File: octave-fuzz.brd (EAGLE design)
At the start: 100 x 81.3 mm, 56 parts, among them T1 2N5089, T2 2N5089, T3 2N5089, T4 2N5089, T5 2N5089

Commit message: optimized layout
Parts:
- moved R5 37.2 mm to (55.9, 47.0), turned to 180 degrees
- moved POT_VOL1 29.0 mm to (72.4, 48.3)
- moved D6 26.8 mm to (72.4, 33.0)
- moved D7 26.8 mm to (67.3, 33.0)
- moved POT_VOL2 26.8 mm to (67.3, 44.5)
- moved R14 25.4 mm to (74.9, 20.3), turned to 90 degrees
- moved POT_GAIN1_2 25.2 mm to (72.4, 55.9), turned to 0 degrees
- moved T2 24.2 mm to (64.8, 58.4)
- moved C3 24.2 mm to (63.5, 64.8)
- moved POT_GAIN1 24.2 mm to (68.6, 62.2)
- moved R21 24.2 mm to (72.4, 69.8)
- moved C7 22.9 mm to (62.2, 72.4)
- moved C9 22.9 mm to (29.2, 29.2), turned to 90 degrees
- moved D5 22.2 mm to (63.5, 38.1)
- moved T3 22.2 mm to (33.0, 63.5)
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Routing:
- net GND: track 265.5 -> 208.3 mm
- net N$5: track 67.4 -> 27.7 mm
- net N$3: track 65.0 -> 36.0 mm
- net +9V: track 257.9 -> 276.9 mm
- net N$26: track 24.8 -> 36.8 mm
- net N$4: track 0.00 -> 11.1 mm
- net N$30: track 10.7 -> 20.9 mm
- net N$23: track 28.8 -> 20.5 mm
- net N$22: track 11.0 -> 17.0 mm
- net N$28: track 23.9 -> 29.8 mm
- net N$2: track 38.4 -> 44.0 mm
- net N$6: track 0.00 -> 4.86 mm
- net N$10: track 17.1 -> 13.3 mm
- net 4.5V: track 22.2 -> 18.6 mm
- net N$14: track 38.4 -> 35.0 mm
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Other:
- board size 100 x 81.3 mm -> 77.1 x 81.3 mm

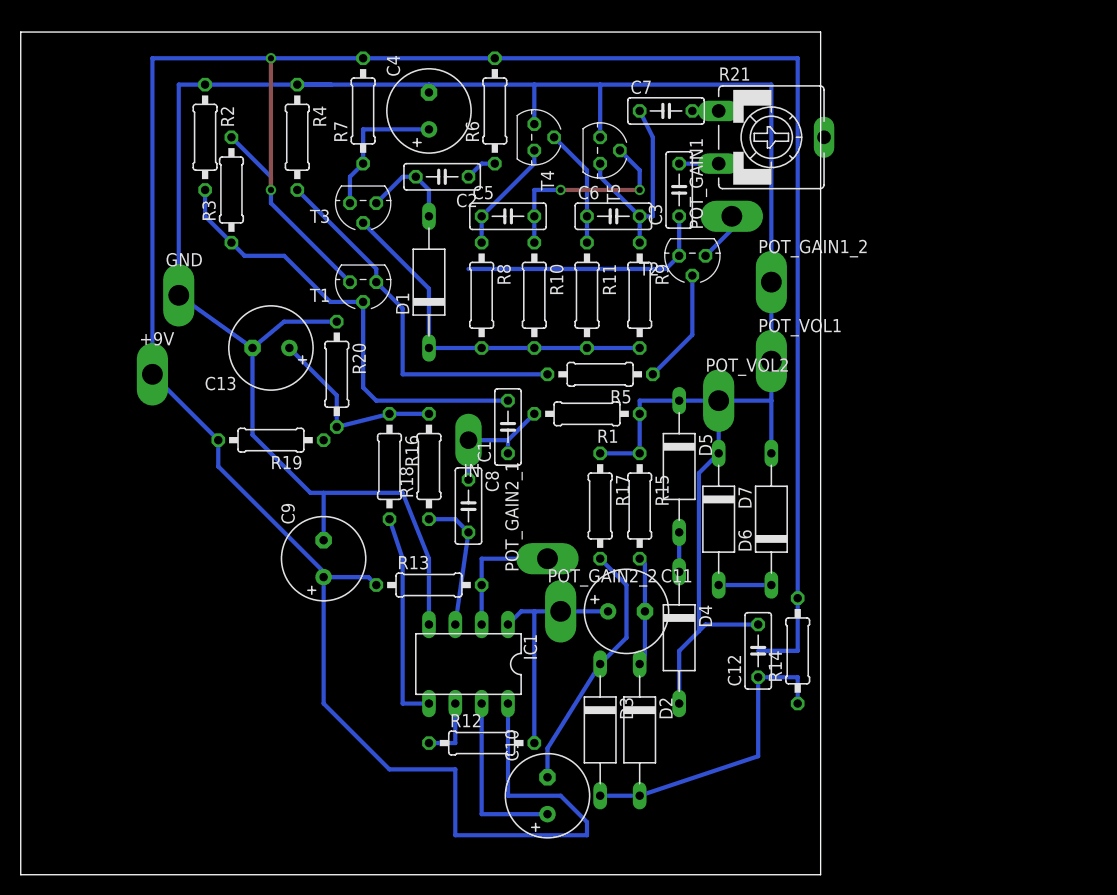
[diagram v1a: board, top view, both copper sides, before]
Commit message: improved pcb layout
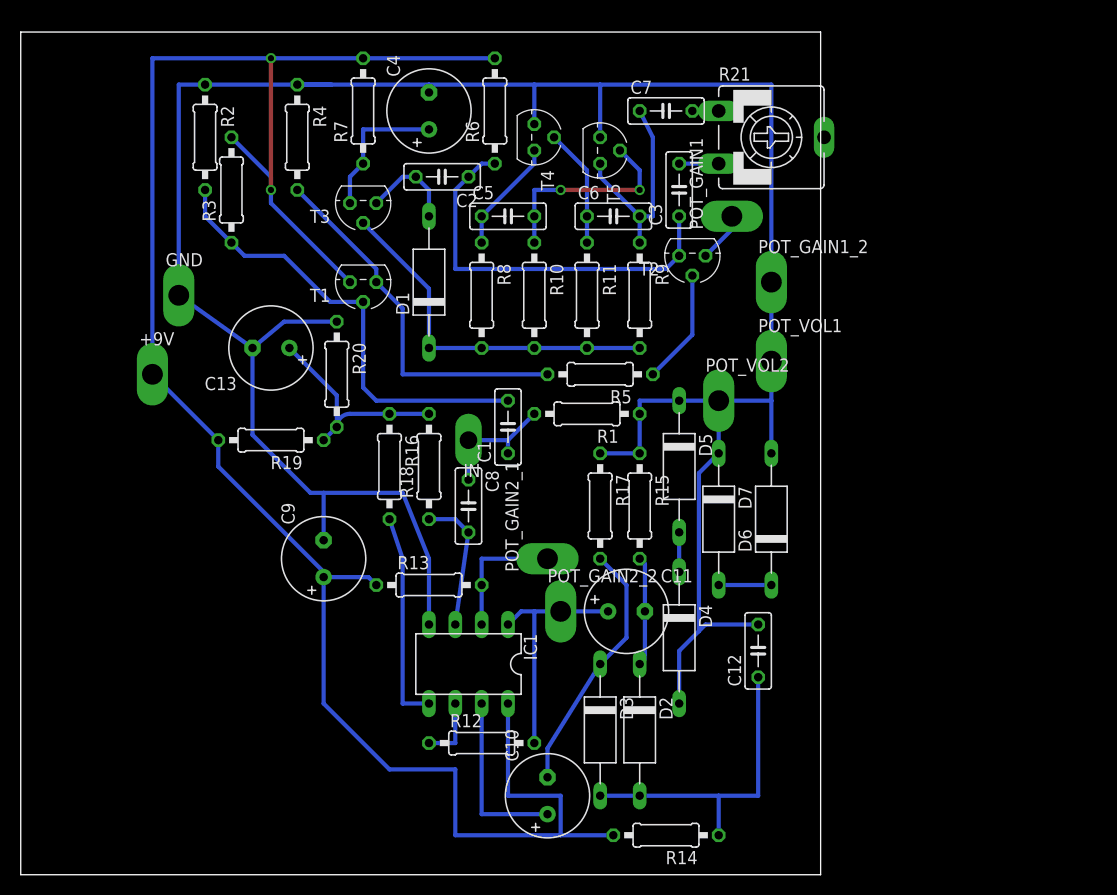
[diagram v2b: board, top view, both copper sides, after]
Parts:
- moved R14 21.8 mm to (62.2, 2.54), turned to 180 degrees
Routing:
- net +9V: track 276.9 -> 188.2 mm
- net N$5: track 27.7 -> 38.4 mm
- net 4.5V: track 18.6 -> 20.7 mm
- net N$28: track 29.8 -> 30.5 mm
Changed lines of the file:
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@@
 <layer number="23" name="tOrigins" color="15" fill="1" visible="yes" active="yes"/>
 <layer number="24" name="bOrigins" color="15" fill="1" visible="yes" active="yes"/>
-<layer number="25" name="tNames" color="7" fill="1" visible="no" active="yes"/>
-<layer number="26" name="bNames" color="7" fill="1" visible="no" active="yes"/>
+<layer number="25" name="tNames" color="7" fill="1" visible="yes" active="yes"/>
+<layer number="26" name="bNames" color="7" fill="1" visible="yes" active="yes"/>
 <layer number="27" name="tValues" color="7" fill="1" visible="no" active="yes"/>
 <layer number="28" name="bValues" color="7" fill="1" visible="no" active="yes"/>
@@
 <element name="R12" library="resistor" package="0207/10" value="" x="44.45" y="11.43"/>
 <element name="R13" library="resistor" package="0207/10" value="" x="39.37" y="26.67"/>
-<element name="R14" library="resistor" package="0207/10" value="" x="74.93" y="20.32" rot="R90"/>
+<element name="R14" library="resistor" package="0207/10" value="" x="62.23" y="2.54" rot="R180"/>
 <element name="R15" library="resistor" package="0207/10" value="" x="59.69" y="34.29" rot="R270"/>
 <element name="R16" library="resistor" package="0207/10" value="" x="35.56" y="38.1" rot="R270"/>
@@
 <wire x1="12.7" y1="46.99" x2="12.7" y2="77.47" width="0.4064" layer="16"/>
 <wire x1="12.7" y1="77.47" x2="24.13" y2="77.47" width="0.4064" layer="16"/>
-<wire x1="24.13" y1="77.47" x2="74.93" y2="77.47" width="0.4064" layer="16"/>
 <via x="24.13" y="64.77" extent="1-16" drill="0.6" shape="square"/>
 <via x="24.13" y="77.47" extent="1-16" drill="0.6" shape="square"/>
 <wire x1="24.13" y1="64.77" x2="24.13" y2="77.47" width="0.4064" layer="1"/>
-<wire x1="74.93" y1="25.4" x2="74.93" y2="77.47" width="0.4064" layer="16"/>
-<wire x1="74.93" y1="25.4" x2="74.93" y2="20.32" width="0.4064" layer="16"/>
-<wire x1="74.93" y1="20.32" x2="71.12" y2="20.32" width="0.4064" layer="16"/>
 <wire x1="31.75" y1="55.88" x2="24.13" y2="63.5" width="0.4064" layer="16"/>
 <wire x1="24.13" y1="63.5" x2="24.13" y2="64.77" width="0.4064" layer="16"/>
@@
 <wire x1="35.56" y1="8.89" x2="41.91" y2="8.89" width="0.4064" layer="16"/>
 <wire x1="41.91" y1="8.89" x2="41.91" y2="2.54" width="0.4064" layer="16"/>
-<wire x1="41.91" y1="2.54" x2="54.61" y2="2.54" width="0.4064" layer="16"/>
-<wire x1="54.61" y1="2.54" x2="54.61" y2="3.81" width="0.4064" layer="16"/>
-<wire x1="54.61" y1="3.81" x2="52.07" y2="6.35" width="0.4064" layer="16"/>
+<wire x1="41.91" y1="2.54" x2="52.07" y2="2.54" width="0.4064" layer="16"/>
+<wire x1="52.07" y1="2.54" x2="52.07" y2="6.35" width="0.4064" layer="16"/>
 <wire x1="52.07" y1="6.35" x2="46.99" y2="6.35" width="0.4064" layer="16"/>
 <wire x1="46.99" y1="6.35" x2="46.99" y2="15.24" width="0.4064" layer="16"/>
@@
 <wire x1="19.05" y1="38.1" x2="29.21" y2="27.94" width="0.4064" layer="16"/>
 <wire x1="29.21" y1="27.94" x2="29.21" y2="15.24" width="0.4064" layer="16"/>
-<wire x1="33.02" y1="77.47" x2="45.72" y2="77.47" width="0" layer="19" extent="1-1"/>
-<wire x1="24.13" y1="77.47" x2="33.02" y2="77.47" width="0" layer="19" extent="16-16"/>
+<wire x1="52.07" y1="2.54" x2="57.15" y2="2.54" width="0.4064" layer="16"/>
+<wire x1="24.13" y1="77.47" x2="33.02" y2="77.47" width="0.4064" layer="16"/>
+<wire x1="33.02" y1="77.47" x2="45.72" y2="77.47" width="0.4064" layer="16"/>
 </signal>
 <signal name="N$2">
@@
 <wire x1="63.5" y1="62.23" x2="63.5" y2="58.42" width="0.4064" layer="16"/>
 <wire x1="63.5" y1="58.42" x2="62.23" y2="57.15" width="0.4064" layer="16"/>
-<wire x1="62.23" y1="57.15" x2="43.18" y2="57.15" width="0.4064" layer="16"/>
+<wire x1="62.23" y1="57.15" x2="41.91" y2="57.15" width="0.4064" layer="16"/>
 <wire x1="43.18" y1="66.04" x2="44.45" y2="67.31" width="0.4064" layer="16"/>
 <wire x1="44.45" y1="67.31" x2="45.72" y2="67.31" width="0.4064" layer="16"/>
-<wire x1="43.18" y1="57.15" x2="43.18" y2="66.04" width="0" layer="19" extent="16-16"/>
+<wire x1="41.91" y1="57.15" x2="41.91" y2="64.77" width="0.4064" layer="16"/>
+<wire x1="41.91" y1="64.77" x2="43.18" y2="66.04" width="0.4064" layer="16"/>
 </signal>
 <signal name="N$6">
@@
 <contactref element="C12" pad="1"/>
 <wire x1="55.88" y1="6.35" x2="59.69" y2="6.35" width="0.4064" layer="16"/>
-<wire x1="59.69" y1="6.35" x2="71.12" y2="10.16" width="0.4064" layer="16"/>
-<wire x1="71.12" y1="10.16" x2="71.12" y2="17.78" width="0.4064" layer="16"/>
-<wire x1="71.12" y1="17.78" x2="74.93" y2="17.78" width="0.4064" layer="16"/>
-<wire x1="74.93" y1="17.78" x2="74.93" y2="15.24" width="0.4064" layer="16"/>
+<wire x1="59.69" y1="6.35" x2="67.31" y2="6.35" width="0.4064" layer="16"/>
+<wire x1="67.31" y1="6.35" x2="71.12" y2="6.35" width="0.4064" layer="16"/>
+<wire x1="71.12" y1="6.35" x2="71.12" y2="17.78" width="0.4064" layer="16"/>
+<wire x1="67.31" y1="2.54" x2="67.31" y2="6.35" width="0.4064" layer="16"/>
 </signal>
 <signal name="N$27">
@@
 <contactref element="R20" pad="2"/>
 <contactref element="C13" pad="+"/>
-<wire x1="35.56" y1="43.18" x2="30.48" y2="41.91" width="0.4064" layer="16"/>
 <wire x1="25.908" y1="49.53" x2="30.48" y2="44.958" width="0.4064" layer="16"/>
 <wire x1="30.48" y1="44.958" x2="30.48" y2="41.91" width="0.4064" layer="16"/>
 <wire x1="35.56" y1="43.18" x2="39.37" y2="43.18" width="0.4064" layer="16"/>
-<wire x1="29.21" y1="40.64" x2="30.48" y2="41.91" width="0" layer="19" extent="1-1"/>
+<wire x1="35.56" y1="43.18" x2="31.75" y2="43.18" width="0.4064" layer="16"/>
+<wire x1="31.75" y1="43.18" x2="30.48" y2="41.91" width="0.4064" layer="16" curve="90"/>
+<wire x1="29.21" y1="40.64" x2="30.48" y2="41.91" width="0.4064" layer="16"/>
 </signal>
 <signal name="N$30">
